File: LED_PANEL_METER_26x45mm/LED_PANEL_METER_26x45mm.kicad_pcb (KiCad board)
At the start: 2 copper layers, 51 x 32 mm, 4 parts

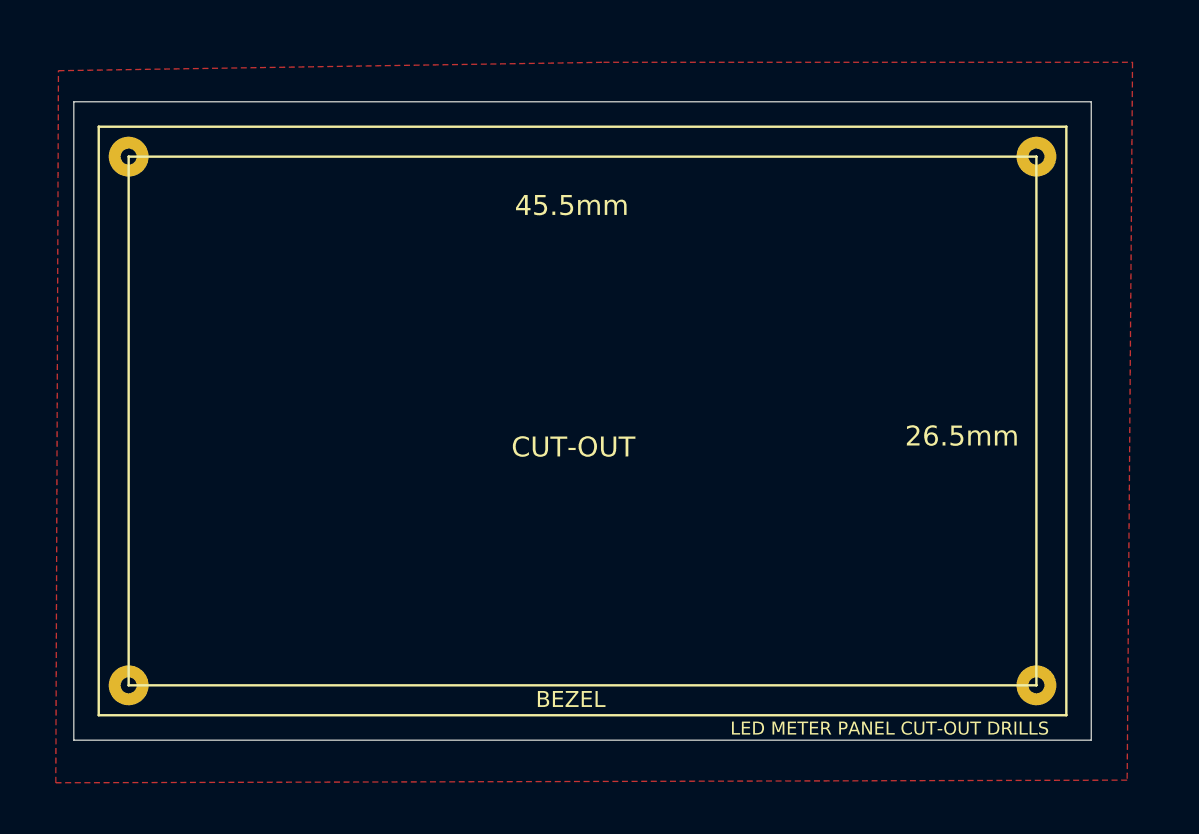
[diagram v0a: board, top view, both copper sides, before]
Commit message: all:(LED_PANEL)renamed files
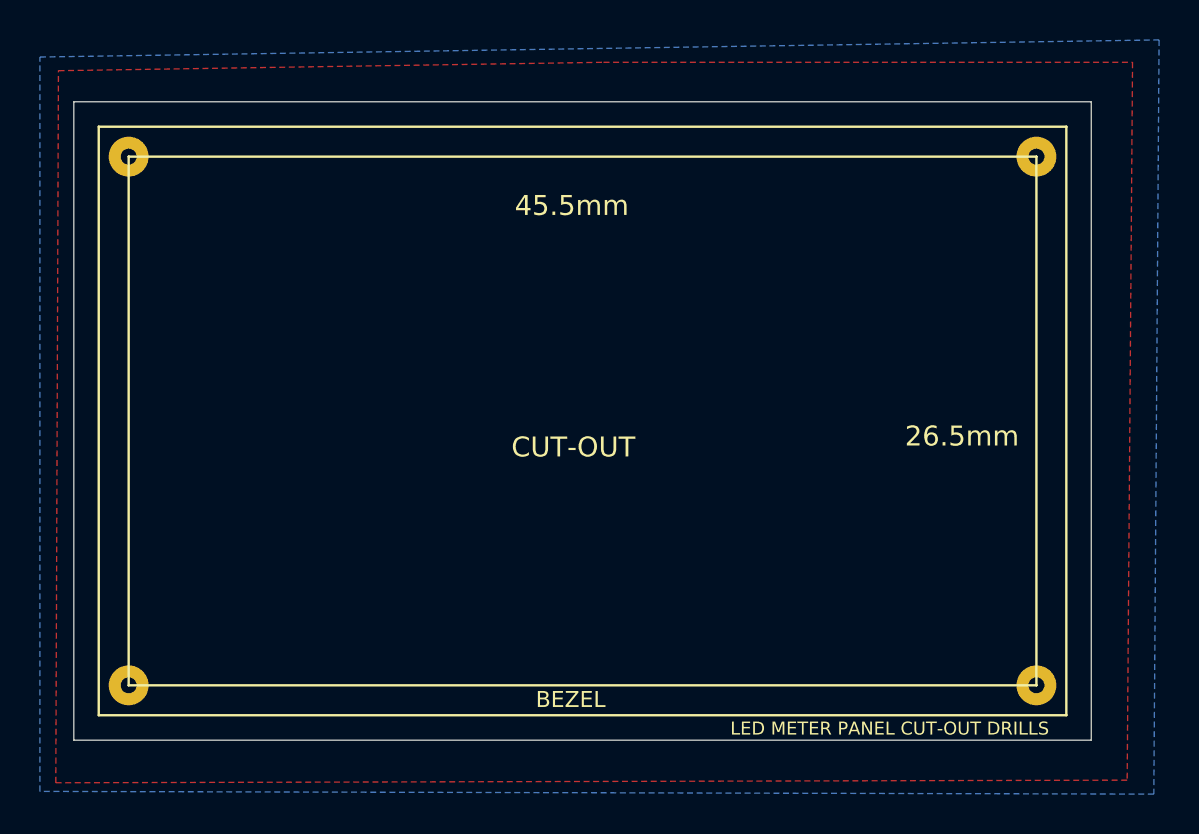
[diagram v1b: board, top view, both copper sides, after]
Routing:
- added copper zone on B.Cu, net (none)
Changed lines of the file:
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@@
   (page A4)
   (title_block
-    (title LED_PANEL_26x45mm)
+    (title LED_PANEL_METER_26x45mm)
     (company Galopago)
   )
@@
       )
     )
+  )
+  (zone (net 0) (net_name "") (layer B.Cu) (hatch edge 0.508)
+    (connect_pads (clearance 0.508))
+    (min_thickness 0.254)
+    (fill yes (arc_segments 32) (thermal_gap 0.508) (thermal_bridge_width 0.508))
+    (polygon
+      (pts
+        (xy 104.13492 84.70392) (xy 48.30064 84.56676) (xy 48.30064 47.75708) (xy 104.39908 46.89856)
+      )
+    )
